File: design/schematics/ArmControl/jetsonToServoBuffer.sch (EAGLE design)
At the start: 3 parts, among them T1 2N3904, T2 2N3904

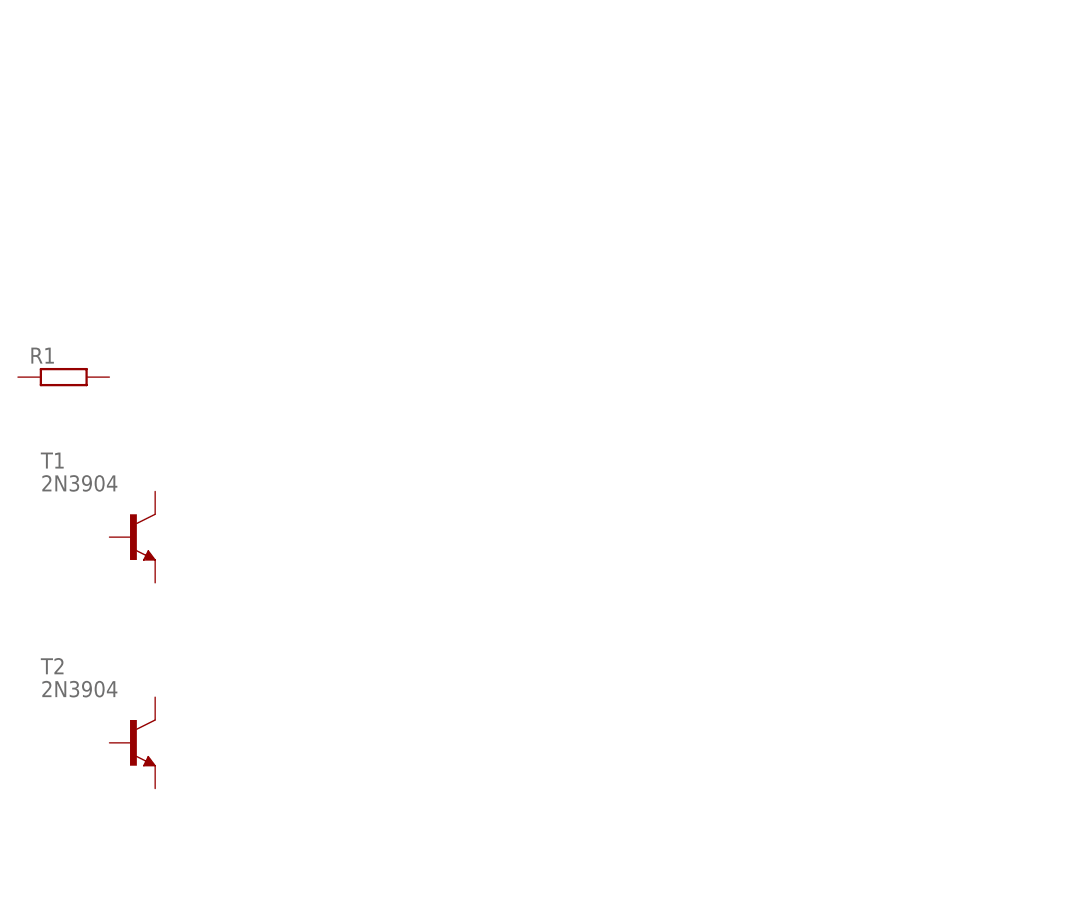
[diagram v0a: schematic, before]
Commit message: updated schematic for buffer between TK1 and servo
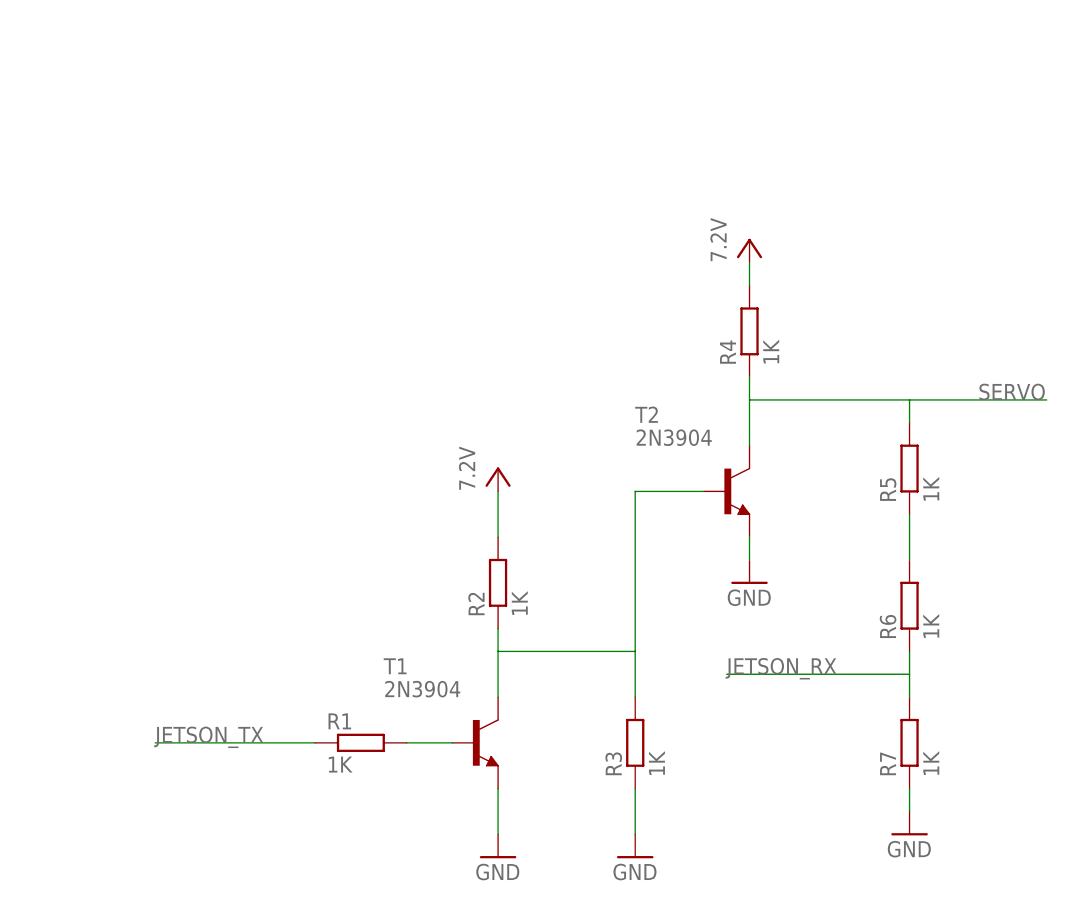
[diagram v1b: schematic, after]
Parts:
- added R2, R3, R4, R5, R6, R7: 1K, resistor:R-EU_0309/10
- R1: value (none) -> 1K
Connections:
- new net GND: R3.1, R7.1, T1.E, T2.E
- new net JETSON_RX: R6.1, R7.2
- new net JETSON_TX: R1.1
- new net N$1: R1.2, T1.B
- new net N$3: R2.1, R3.2, T1.C, T2.B
- new net N$5: R5.1, R6.2
- new net SERVO: R4.1, R5.2, T2.C
- new net VCC: R2.2, R4.2
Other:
- moved on the sheet: R1, T1, T2
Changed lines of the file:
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@@
 <part name="T1" library="transistor" deviceset="2N3904" device=""/>
 <part name="T2" library="transistor" deviceset="2N3904" device=""/>
-<part name="R1" library="resistor" deviceset="R-EU_" device="0309/10"/>
+<part name="R1" library="resistor" deviceset="R-EU_" device="0309/10" value="1K"/>
+<part name="GND1" library="supply1" deviceset="GND" device=""/>
+<part name="P+1" library="supply1" deviceset="VCC" device="" value="7.2V"/>
+<part name="R2" library="resistor" deviceset="R-EU_" device="0309/10" value="1K"/>
+<part name="R3" library="resistor" deviceset="R-EU_" device="0309/10" value="1K"/>
+<part name="GND2" library="supply1" deviceset="GND" device=""/>
+<part name="R4" library="resistor" deviceset="R-EU_" device="0309/10" value="1K"/>
+<part name="R5" library="resistor" deviceset="R-EU_" device="0309/10" value="1K"/>
+<part name="R6" library="resistor" deviceset="R-EU_" device="0309/10" value="1K"/>
+<part name="R7" library="resistor" deviceset="R-EU_" device="0309/10" value="1K"/>
+<part name="GND3" library="supply1" deviceset="GND" device=""/>
+<part name="GND4" library="supply1" deviceset="GND" device=""/>
+<part name="P+2" library="supply1" deviceset="VCC" device="" value="7.2V"/>
+<part name="FRAME2" library="frames" deviceset="DINA5_L" device=""/>
 </parts>
 <sheets>
@@
 </plain>
 <instances>
-<instance part="T1" gate="G1" x="35.56" y="68.58"/>
-<instance part="T2" gate="G1" x="35.56" y="45.72"/>
-<instance part="R1" gate="G$1" x="27.94" y="86.36"/>
+<instance part="T1" gate="G1" x="73.66" y="45.72"/>
+<instance part="T2" gate="G1" x="101.6" y="73.66"/>
+<instance part="R1" gate="G$1" x="60.96" y="45.72"/>
+<instance part="GND1" gate="1" x="76.2" y="33.02"/>
+<instance part="P+1" gate="VCC" x="76.2" y="76.2"/>
+<instance part="R2" gate="G$1" x="76.2" y="63.5" rot="R90"/>
+<instance part="R3" gate="G$1" x="91.44" y="45.72" rot="R90"/>
+<instance part="GND2" gate="1" x="91.44" y="33.02"/>
+<instance part="R4" gate="G$1" x="104.14" y="91.44" rot="R90"/>
+<instance part="R5" gate="G$1" x="121.92" y="76.2" rot="R90"/>
+<instance part="R6" gate="G$1" x="121.92" y="60.96" rot="R90"/>
+<instance part="R7" gate="G$1" x="121.92" y="45.72" rot="R90"/>
+<instance part="GND3" gate="1" x="104.14" y="63.5"/>
+<instance part="GND4" gate="1" x="121.92" y="35.56"/>
+<instance part="P+2" gate="VCC" x="104.14" y="101.6"/>
+<instance part="FRAME2" gate="G$1" x="0" y="0"/>
 </instances>
 <busses>
 </busses>
 <nets>
+<net name="N$1" class="0">
+<segment>
+<pinref part="T1" gate="G1" pin="B"/>
+<pinref part="R1" gate="G$1" pin="2"/>
+<wire x1="66.04" y1="45.72" x2="71.12" y2="45.72" width="0.1524" layer="91"/>
+</segment>
+</net>
+<net name="GND" class="0">
+<segment>
+<pinref part="T1" gate="G1" pin="E"/>
+<pinref part="GND1" gate="1" pin="GND"/>
+<wire x1="76.2" y1="35.56" x2="76.2" y2="40.64" width="0.1524" layer="91"/>
+</segment>
+<segment>
+<pinref part="R3" gate="G$1" pin="1"/>
+<pinref part="GND2" gate="1" pin="GND"/>
+<wire x1="91.44" y1="35.56" x2="91.44" y2="40.64" width="0.1524" layer="91"/>
+</segment>
+<segment>
+<pinref part="T2" gate="G1" pin="E"/>
+<pinref part="GND3" gate="1" pin="GND"/>
+<wire x1="104.14" y1="66.04" x2="104.14" y2="68.58" width="0.1524" layer="91"/>
+</segment>
+<segment>
+<pinref part="R7" gate="G$1" pin="1"/>
+<pinref part="GND4" gate="1" pin="GND"/>
+<wire x1="121.92" y1="38.1" x2="121.92" y2="40.64" width="0.1524" layer="91"/>
+</segment>
+</net>
+<net name="JETSON_TX" class="0">
+<segment>
+<pinref part="R1" gate="G$1" pin="1"/>
+<wire x1="55.88" y1="45.72" x2="38.1" y2="45.72" width="0.1524" layer="91"/>
+<label x="38.1" y="45.72" size="1.778" layer="95"/>
+</segment>
+</net>
+<net name="N$3" class="0">
+<segment>
+<pinref part="T1" gate="G1" pin="C"/>
+<pinref part="R2" gate="G$1" pin="1"/>
+<wire x1="76.2" y1="58.42" x2="76.2" y2="55.88" width="0.1524" layer="91"/>
+<pinref part="R3" gate="G$1" pin="2"/>
+<wire x1="76.2" y1="55.88" x2="76.2" y2="50.8" width="0.1524" layer="91"/>
+<wire x1="76.2" y1="55.88" x2="91.44" y2="55.88" width="0.1524" layer="91"/>
+<wire x1="91.44" y1="55.88" x2="91.44" y2="50.8" width="0.1524" layer="91"/>
+<pinref part="T2" gate="G1" pin="B"/>
+<wire x1="91.44" y1="55.88" x2="91.44" y2="73.66" width="0.1524" layer="91"/>
+<wire x1="91.44" y1="73.66" x2="99.06" y2="73.66" width="0.1524" layer="91"/>
+</segment>
+</net>
+<net name="VCC" class="0">
+<segment>
+<pinref part="P+1" gate="VCC" pin="VCC"/>
+<pinref part="R2" gate="G$1" pin="2"/>
+<wire x1="76.2" y1="68.58" x2="76.2" y2="73.66" width="0.1524" layer="91"/>
+</segment>
+<segment>
+<pinref part="R4" gate="G$1" pin="2"/>
+<pinref part="P+2" gate="VCC" pin="VCC"/>
+<wire x1="104.14" y1="99.06" x2="104.14" y2="96.52" width="0.1524" layer="91"/>
+</segment>
+</net>
+<net name="JETSON_RX" class="0">
+<segment>
+<pinref part="R7" gate="G$1" pin="2"/>
+<pinref part="R6" gate="G$1" pin="1"/>
+<wire x1="121.92" y1="55.88" x2="121.92" y2="53.34" width="0.1524" layer="91"/>
+<wire x1="121.92" y1="53.34" x2="121.92" y2="50.8" width="0.1524" layer="91"/>
+<wire x1="121.92" y1="53.34" x2="101.6" y2="53.34" width="0.1524" layer="91"/>
+<label x="101.6" y="53.34" size="1.778" layer="95"/>
+</segment>
+</net>
+<net name="N$5" class="0">
+<segment>
+<pinref part="R5" gate="G$1" pin="1"/>
+<pinref part="R6" gate="G$1" pin="2"/>
+<wire x1="121.92" y1="66.04" x2="121.92" y2="71.12" width="0.1524" layer="91"/>
+</segment>
+</net>
+<net name="SERVO" class="0">
+<segment>
+<pinref part="R4" gate="G$1" pin="1"/>
+<pinref part="T2" gate="G1" pin="C"/>
+<wire x1="104.14" y1="86.36" x2="104.14" y2="83.82" width="0.1524" layer="91"/>
+<pinref part="R5" gate="G$1" pin="2"/>
+<wire x1="104.14" y1="83.82" x2="104.14" y2="78.74" width="0.1524" layer="91"/>
+<wire x1="121.92" y1="81.28" x2="121.92" y2="83.82" width="0.1524" layer="91"/>
+<wire x1="121.92" y1="83.82" x2="104.14" y2="83.82" width="0.1524" layer="91"/>
+<wire x1="121.92" y1="83.82" x2="137.16" y2="83.82" width="0.1524" layer="91"/>
+<label x="129.54" y="83.82" size="1.778" layer="95"/>
+</segment>
+</net>
 </nets>
 </sheet>

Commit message: updated schematic to make it simpler and still work
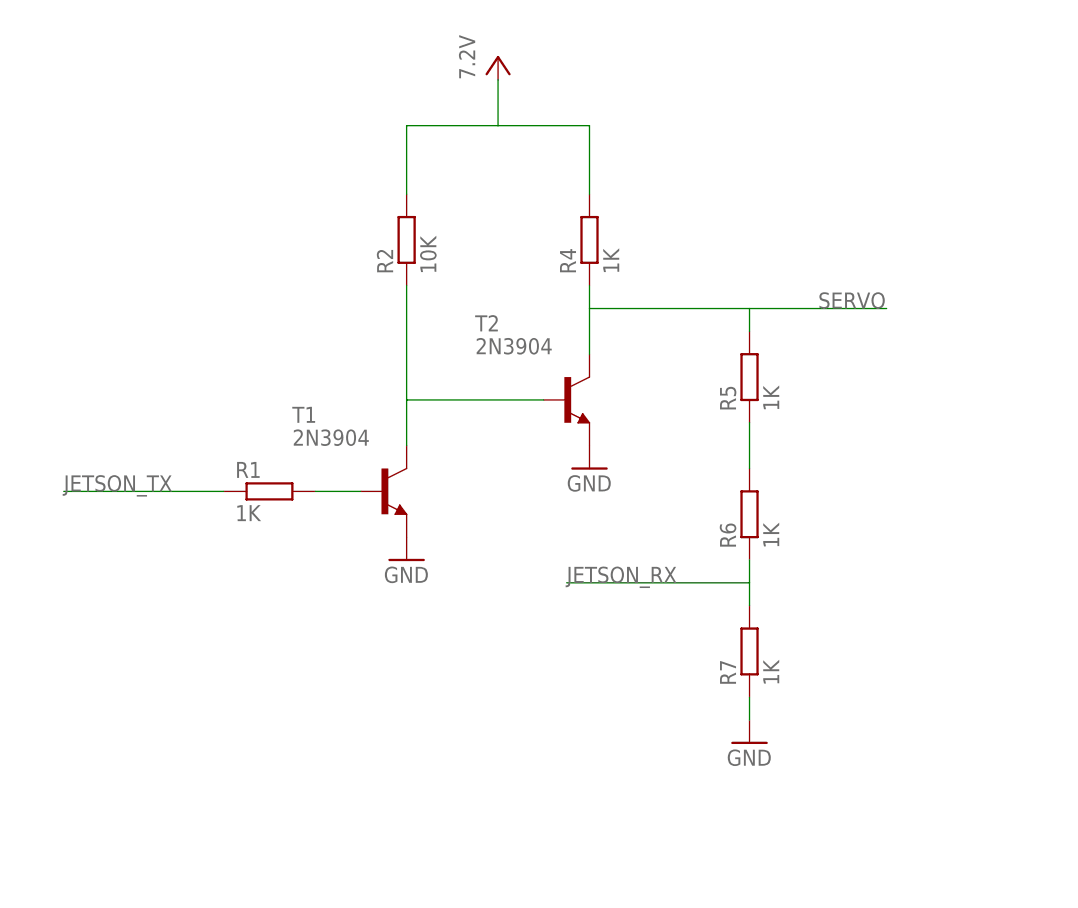
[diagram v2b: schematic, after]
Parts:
- removed R3: 1K, resistor:R-EU_0309/10
- R2: value 1K -> 10K
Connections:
- net GND: no longer R3.1
- net N$3: no longer R3.2
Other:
- moved on the sheet: R1, R2, R4, R5, R6, R7, T1, T2
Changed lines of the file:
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@@
 <part name="GND1" library="supply1" deviceset="GND" device=""/>
 <part name="P+1" library="supply1" deviceset="VCC" device="" value="7.2V"/>
-<part name="R2" library="resistor" deviceset="R-EU_" device="0309/10" value="1K"/>
-<part name="R3" library="resistor" deviceset="R-EU_" device="0309/10" value="1K"/>
-<part name="GND2" library="supply1" deviceset="GND" device=""/>
+<part name="R2" library="resistor" deviceset="R-EU_" device="0309/10" value="10K"/>
 <part name="R4" library="resistor" deviceset="R-EU_" device="0309/10" value="1K"/>
 <part name="R5" library="resistor" deviceset="R-EU_" device="0309/10" value="1K"/>
@@
 <part name="GND3" library="supply1" deviceset="GND" device=""/>
 <part name="GND4" library="supply1" deviceset="GND" device=""/>
-<part name="P+2" library="supply1" deviceset="VCC" device="" value="7.2V"/>
 <part name="FRAME2" library="frames" deviceset="DINA5_L" device=""/>
 </parts>
@@
 </plain>
 <instances>
-<instance part="T1" gate="G1" x="73.66" y="45.72"/>
-<instance part="T2" gate="G1" x="101.6" y="73.66"/>
-<instance part="R1" gate="G$1" x="60.96" y="45.72"/>
-<instance part="GND1" gate="1" x="76.2" y="33.02"/>
-<instance part="P+1" gate="VCC" x="76.2" y="76.2"/>
-<instance part="R2" gate="G$1" x="76.2" y="63.5" rot="R90"/>
-<instance part="R3" gate="G$1" x="91.44" y="45.72" rot="R90"/>
-<instance part="GND2" gate="1" x="91.44" y="33.02"/>
-<instance part="R4" gate="G$1" x="104.14" y="91.44" rot="R90"/>
-<instance part="R5" gate="G$1" x="121.92" y="76.2" rot="R90"/>
-<instance part="R6" gate="G$1" x="121.92" y="60.96" rot="R90"/>
-<instance part="R7" gate="G$1" x="121.92" y="45.72" rot="R90"/>
-<instance part="GND3" gate="1" x="104.14" y="63.5"/>
-<instance part="GND4" gate="1" x="121.92" y="35.56"/>
-<instance part="P+2" gate="VCC" x="104.14" y="101.6"/>
+<instance part="T1" gate="G1" x="63.5" y="73.66"/>
+<instance part="T2" gate="G1" x="83.82" y="83.82"/>
+<instance part="R1" gate="G$1" x="50.8" y="73.66"/>
+<instance part="GND1" gate="1" x="66.04" y="66.04"/>
+<instance part="P+1" gate="VCC" x="76.2" y="121.92"/>
+<instance part="R2" gate="G$1" x="66.04" y="101.6" rot="R90"/>
+<instance part="R4" gate="G$1" x="86.36" y="101.6" rot="R90"/>
+<instance part="R5" gate="G$1" x="104.14" y="86.36" rot="R90"/>
+<instance part="R6" gate="G$1" x="104.14" y="71.12" rot="R90"/>
+<instance part="R7" gate="G$1" x="104.14" y="55.88" rot="R90"/>
+<instance part="GND3" gate="1" x="86.36" y="76.2"/>
+<instance part="GND4" gate="1" x="104.14" y="45.72"/>
 <instance part="FRAME2" gate="G$1" x="0" y="0"/>
 </instances>
@@
 <pinref part="T1" gate="G1" pin="B"/>
 <pinref part="R1" gate="G$1" pin="2"/>
-<wire x1="66.04" y1="45.72" x2="71.12" y2="45.72" width="0.1524" layer="91"/>
+<wire x1="55.88" y1="73.66" x2="60.96" y2="73.66" width="0.1524" layer="91"/>
 </segment>
 </net>
@@
 <pinref part="T1" gate="G1" pin="E"/>
 <pinref part="GND1" gate="1" pin="GND"/>
-<wire x1="76.2" y1="35.56" x2="76.2" y2="40.64" width="0.1524" layer="91"/>
-</segment>
-<segment>
-<pinref part="R3" gate="G$1" pin="1"/>
-<pinref part="GND2" gate="1" pin="GND"/>
-<wire x1="91.44" y1="35.56" x2="91.44" y2="40.64" width="0.1524" layer="91"/>
 </segment>
 <segment>
 <pinref part="T2" gate="G1" pin="E"/>
 <pinref part="GND3" gate="1" pin="GND"/>
-<wire x1="104.14" y1="66.04" x2="104.14" y2="68.58" width="0.1524" layer="91"/>
 </segment>
 <segment>
 <pinref part="R7" gate="G$1" pin="1"/>
 <pinref part="GND4" gate="1" pin="GND"/>
-<wire x1="121.92" y1="38.1" x2="121.92" y2="40.64" width="0.1524" layer="91"/>
+<wire x1="104.14" y1="48.26" x2="104.14" y2="50.8" width="0.1524" layer="91"/>
 </segment>
 </net>
@@
 <segment>
 <pinref part="R1" gate="G$1" pin="1"/>
-<wire x1="55.88" y1="45.72" x2="38.1" y2="45.72" width="0.1524" layer="91"/>
-<label x="38.1" y="45.72" size="1.778" layer="95"/>
+<wire x1="45.72" y1="73.66" x2="27.94" y2="73.66" width="0.1524" layer="91"/>
+<label x="27.94" y="73.66" size="1.778" layer="95"/>
 </segment>
 </net>
@@
 <pinref part="T1" gate="G1" pin="C"/>
 <pinref part="R2" gate="G$1" pin="1"/>
-<wire x1="76.2" y1="58.42" x2="76.2" y2="55.88" width="0.1524" layer="91"/>
-<pinref part="R3" gate="G$1" pin="2"/>
-<wire x1="76.2" y1="55.88" x2="76.2" y2="50.8" width="0.1524" layer="91"/>
-<wire x1="76.2" y1="55.88" x2="91.44" y2="55.88" width="0.1524" layer="91"/>
-<wire x1="91.44" y1="55.88" x2="91.44" y2="50.8" width="0.1524" layer="91"/>
+<wire x1="66.04" y1="96.52" x2="66.04" y2="83.82" width="0.1524" layer="91"/>
+<wire x1="66.04" y1="83.82" x2="66.04" y2="78.74" width="0.1524" layer="91"/>
+<wire x1="66.04" y1="83.82" x2="81.28" y2="83.82" width="0.1524" layer="91"/>
 <pinref part="T2" gate="G1" pin="B"/>
-<wire x1="91.44" y1="55.88" x2="91.44" y2="73.66" width="0.1524" layer="91"/>
-<wire x1="91.44" y1="73.66" x2="99.06" y2="73.66" width="0.1524" layer="91"/>
 </segment>
 </net>
@@
 <pinref part="P+1" gate="VCC" pin="VCC"/>
 <pinref part="R2" gate="G$1" pin="2"/>
-<wire x1="76.2" y1="68.58" x2="76.2" y2="73.66" width="0.1524" layer="91"/>
-</segment>
-<segment>
+<wire x1="66.04" y1="106.68" x2="66.04" y2="114.3" width="0.1524" layer="91"/>
+<wire x1="66.04" y1="114.3" x2="76.2" y2="114.3" width="0.1524" layer="91"/>
+<wire x1="76.2" y1="114.3" x2="76.2" y2="119.38" width="0.1524" layer="91"/>
 <pinref part="R4" gate="G$1" pin="2"/>
-<pinref part="P+2" gate="VCC" pin="VCC"/>
-<wire x1="104.14" y1="99.06" x2="104.14" y2="96.52" width="0.1524" layer="91"/>
+<wire x1="76.2" y1="114.3" x2="86.36" y2="114.3" width="0.1524" layer="91"/>
+<wire x1="86.36" y1="114.3" x2="86.36" y2="106.68" width="0.1524" layer="91"/>
 </segment>
 </net>
@@
 <pinref part="R7" gate="G$1" pin="2"/>
 <pinref part="R6" gate="G$1" pin="1"/>
-<wire x1="121.92" y1="55.88" x2="121.92" y2="53.34" width="0.1524" layer="91"/>
-<wire x1="121.92" y1="53.34" x2="121.92" y2="50.8" width="0.1524" layer="91"/>
-<wire x1="121.92" y1="53.34" x2="101.6" y2="53.34" width="0.1524" layer="91"/>
-<label x="101.6" y="53.34" size="1.778" layer="95"/>
+<wire x1="104.14" y1="66.04" x2="104.14" y2="63.5" width="0.1524" layer="91"/>
+<wire x1="104.14" y1="63.5" x2="104.14" y2="60.96" width="0.1524" layer="91"/>
+<wire x1="104.14" y1="63.5" x2="83.82" y2="63.5" width="0.1524" layer="91"/>
+<label x="83.82" y="63.5" size="1.778" layer="95"/>
 </segment>
 </net>
@@
 <pinref part="R5" gate="G$1" pin="1"/>
 <pinref part="R6" gate="G$1" pin="2"/>
-<wire x1="121.92" y1="66.04" x2="121.92" y2="71.12" width="0.1524" layer="91"/>
+<wire x1="104.14" y1="76.2" x2="104.14" y2="81.28" width="0.1524" layer="91"/>
 </segment>
 </net>
@@
 <pinref part="R4" gate="G$1" pin="1"/>
 <pinref part="T2" gate="G1" pin="C"/>
-<wire x1="104.14" y1="86.36" x2="104.14" y2="83.82" width="0.1524" layer="91"/>
+<wire x1="86.36" y1="96.52" x2="86.36" y2="93.98" width="0.1524" layer="91"/>
 <pinref part="R5" gate="G$1" pin="2"/>
-<wire x1="104.14" y1="83.82" x2="104.14" y2="78.74" width="0.1524" layer="91"/>
-<wire x1="121.92" y1="81.28" x2="121.92" y2="83.82" width="0.1524" layer="91"/>
-<wire x1="121.92" y1="83.82" x2="104.14" y2="83.82" width="0.1524" layer="91"/>
-<wire x1="121.92" y1="83.82" x2="137.16" y2="83.82" width="0.1524" layer="91"/>
-<label x="129.54" y="83.82" size="1.778" layer="95"/>
+<wire x1="86.36" y1="93.98" x2="86.36" y2="88.9" width="0.1524" layer="91"/>
+<wire x1="104.14" y1="91.44" x2="104.14" y2="93.98" width="0.1524" layer="91"/>
+<wire x1="104.14" y1="93.98" x2="86.36" y2="93.98" width="0.1524" layer="91"/>
+<wire x1="104.14" y1="93.98" x2="119.38" y2="93.98" width="0.1524" layer="91"/>
+<label x="111.76" y="93.98" size="1.778" layer="95"/>
 </segment>
 </net>
